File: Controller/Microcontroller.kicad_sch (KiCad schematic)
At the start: 35 parts, among them J1 SWD Connector, J13 USB_B_Micro, SW1 SW_Push, SW2 SW_SPDT, SW3 SW_SPDT, U1 STM32F446RCTx, U5 TVS0500DRV, Y1 25 MHz

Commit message: Reorganize controller schematic
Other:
- title: MCU A - STM32F446RCT6 -> Microcontroller - STM32F446RCTx
- moved on the sheet: C11, C12, C25, D2, FL1, J13, R10, R11, R3, R6, R7, U5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

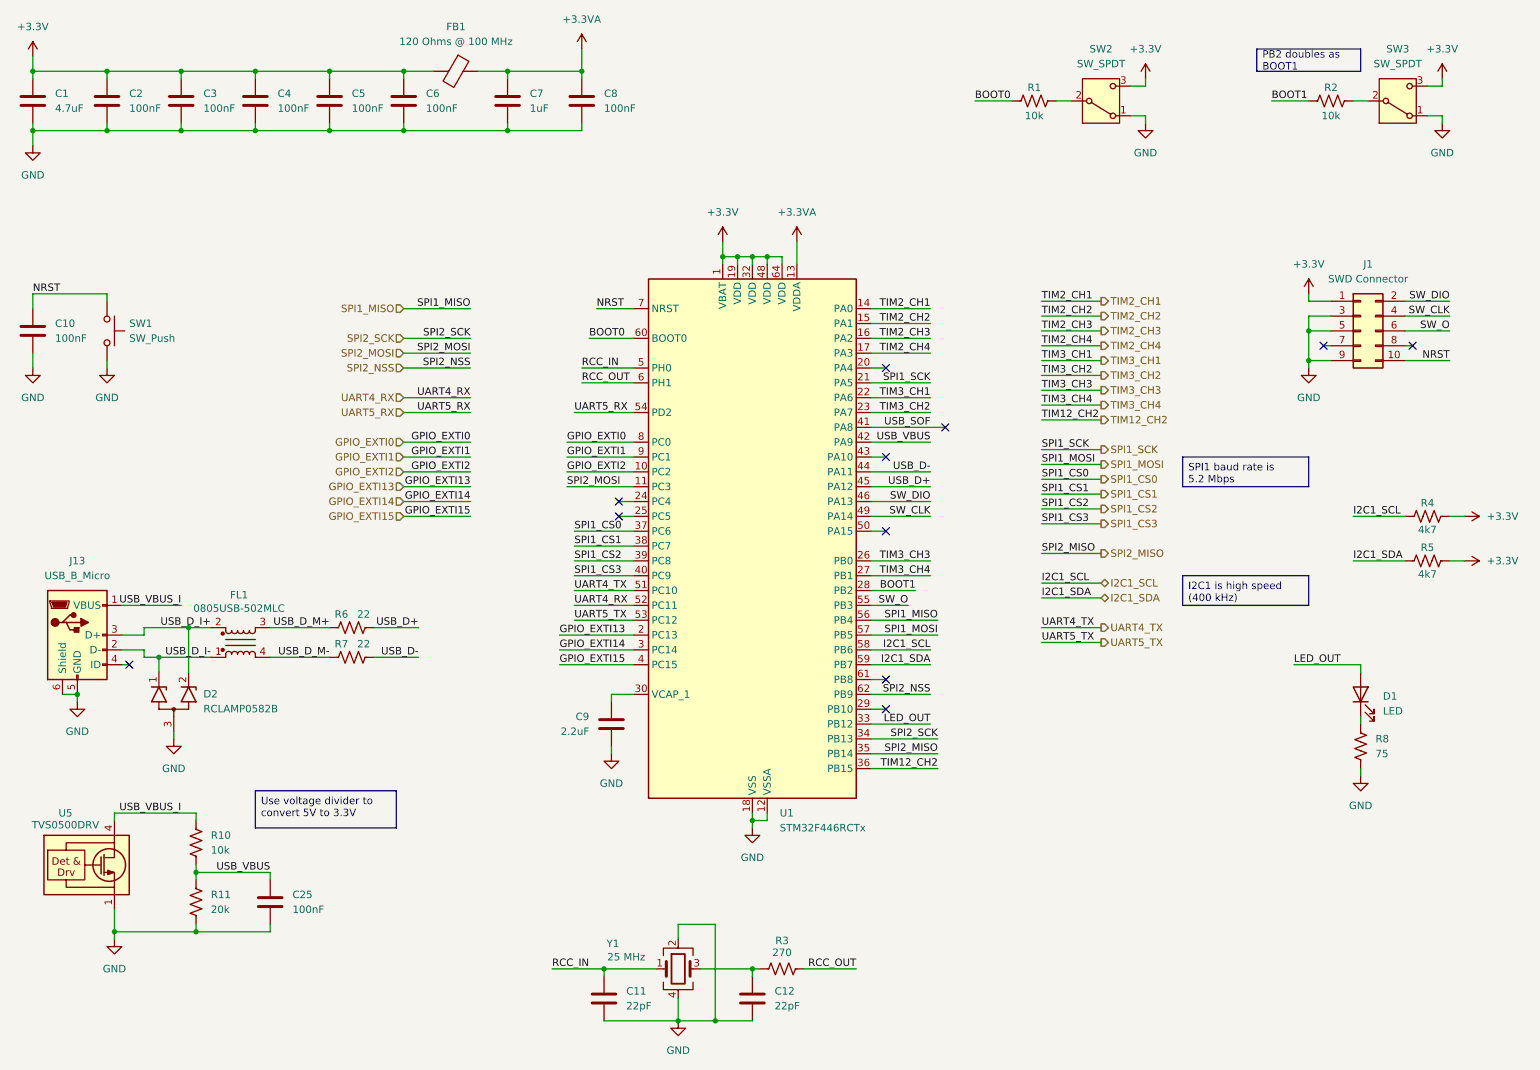
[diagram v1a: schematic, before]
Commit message: Re-number components in controller schematic
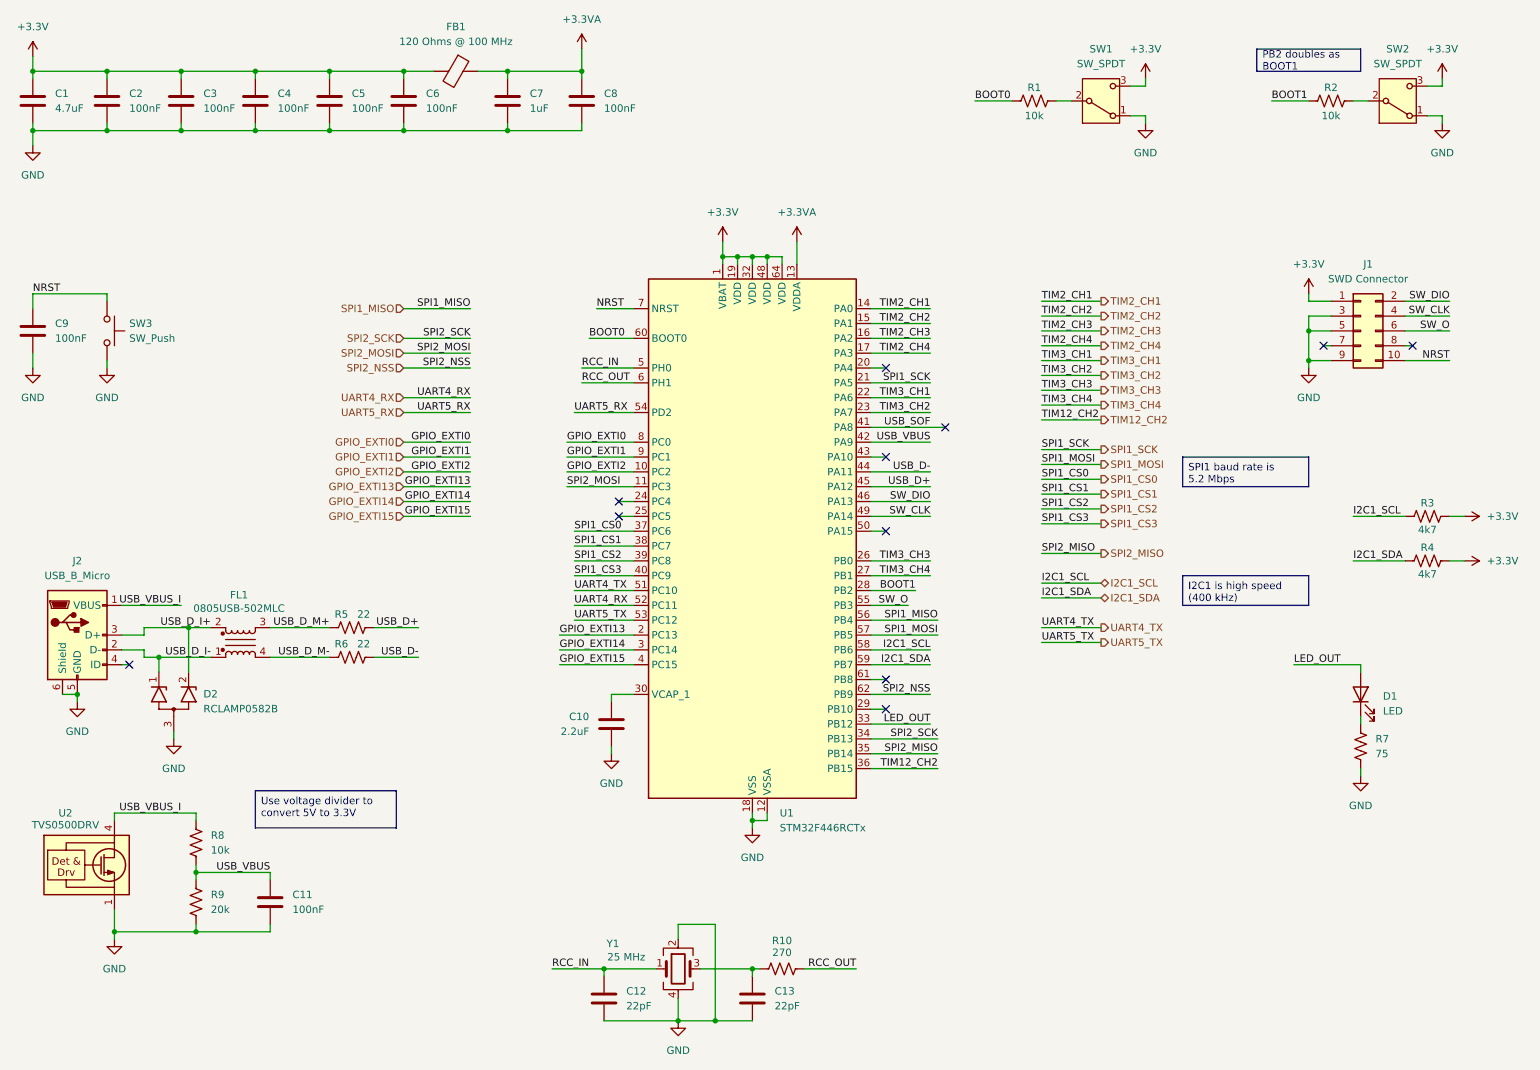
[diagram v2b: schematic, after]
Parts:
- renumbered C9 to C10, C25 to C11, C11 to C12, C12 to C13, C10 to C9, J13 to J2, R3 to R10, R4 to R3, R5 to R4, R6 to R5, R7 to R6, R8 to R7, R10 to R8, R11 to R9, SW2 to SW1, SW3 to SW2, SW1 to SW3, U5 to U2

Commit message: Add power input connector to controller schematic
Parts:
- renumbered C7 to C10, C8 to C11, C9 to C12, C10 to C13, C11 to C14, C12 to C15, C13 to C16, C1 to C4, C2 to C5, C3 to C6, C4 to C7, C5 to C8, C6 to C9, J1 to J2, J2 to J3
